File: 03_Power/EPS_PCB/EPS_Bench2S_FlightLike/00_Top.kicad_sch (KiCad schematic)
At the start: 0 parts

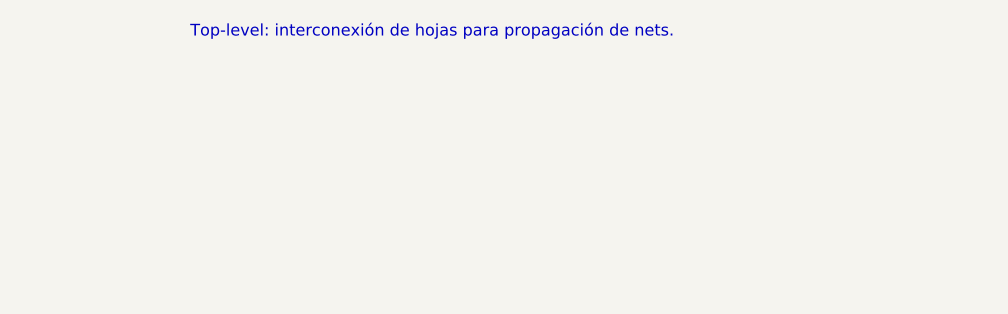
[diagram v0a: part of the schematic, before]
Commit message: EPS: lock unsafe KiCad placeholder
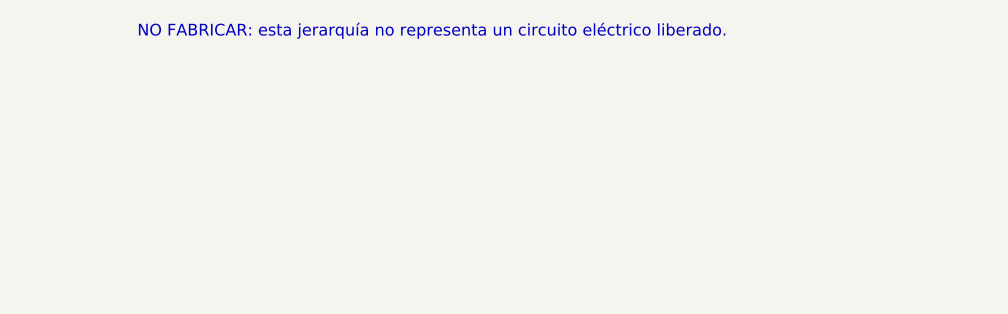
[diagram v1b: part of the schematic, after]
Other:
- note added: "NO FABRICAR: esta jerarquía no representa un circuito eléctrico liberado."
- note removed: "Top-level: interconexión de hojas para propagación de nets."
- title: EPS Bench 2S - Top -> EPS 2S NON-FABRICABLE PLACEHOLDER
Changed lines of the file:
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@@
 	(paper "A4")
 	(title_block
-		(title "EPS Bench 2S - Top")
-		(comment 1 "Interconexión jerárquica")
+		(title "EPS 2S NON-FABRICABLE PLACEHOLDER")
+		(comment 1 "NO FABRICAR / INTERFACES NO IMPLEMENTADAS")
 	)
-	(text "Top-level: interconexión de hojas para propagación de nets."
+	(text "NO FABRICAR: esta jerarquía no representa un circuito eléctrico liberado."
 		(exclude_from_sim no)
 		(at -19.558 -9.398 0)
